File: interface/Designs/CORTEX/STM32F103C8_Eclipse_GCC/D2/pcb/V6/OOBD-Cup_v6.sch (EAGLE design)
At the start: 42 parts, among them IC1 MC34063-SO, IC2 BTM-182, IC3 PCA82C250T, T1 BC817, T100 BC817, T101 BC817, U1 STM32F10XTXU6

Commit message: K-Line interface connected
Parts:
- removed C10: 220pF, rcl:C-EUC0603K
- removed C6: 1µF, rcl:C-EUC0603K
- removed C8: 47µ/35V, cap-master:CP-SV-D
- removed C9: 100nF, rcl:C-EUC0603K
- removed D101: B140, diode:SCHOTTKY-DIODESMD
- removed D102: 1N4148, diode:DIODE-MINIMELF
- removed JP3-OBD1: (no value), jumper:JP4E
- removed L3: 47µH, Inductor-Fastron:07HCP-XXXX-50
- removed L4: 47uH, Inductor-Fastron:PIS2408
- removed R100, R102: 82R, rcl:R-EU_R0603
- removed R104, R109: 4k7, rcl:R-EU_R0603
- removed R108: 10k, rcl:R-EU_R0603
- removed T101: BC817, transistor:BC847
- removed U$1: SI9241AEY, Si9241AEY:SI9241AEY
- added C1: 1µF, rcl:C-EUC0603K
- added C2: 220µF, rc-master:CP_6032-TE-C
- added C3: 220pF, rcl:C-EUC0603K
- added C4: 47µ/35V, cap-master:CP-SV-D
- added C5: 100nF, rcl:C-EUC0603K
- added D2: B140, diode:SCHOTTKY-DIODESMD
- added D3: BAS40, diode:BAS40
- added IC$2: SI9243AEY, Vishay_ISO9141:SI9243AEY
- added JP3: (no value), jumper:JP1E
- added L1: 47uH, Inductor-Fastron:PIS2408
- added L2: 47µH, Inductor-Fastron:07HCP-XXXX-50
- added R11: 3k3, rcl:R-EU_R0603
- added R12, R13, R14: 1R, rcl:R-EU_R0805
- added R15: 5k6, rcl:R-EU_R0603
- added R16: 120R, resistor:R-EU_R0603
- added R18: 510R, resistor:R-EU_R0603
- added T2: BC817, transistor:BC847
- C7: value 220µF -> 10nF; device rc-master:CP_6032-TE-C -> resistor:C-EUC0603
- D1: value BAS40 -> 1N4148; device diode:BAS40 -> diode:DIODE-MINIMELF
- IC1: value MC34063-SO -> PCA82C250T; device mc34063:MC34063-SO -> can:PCA82C250T
- IC3: value PCA82C250T -> MC34063-SO; device can:PCA82C250T -> mc34063:MC34063-SO
- JP1: value SPI / SD-Card -> Program
- JP2: value Program -> SPI / SD-Card
- LED1: value Rt/Gr -> Blue; device led:DUOLED2X5 -> led:LEDSQR5.7X3.2
- LED2: value Blue -> Rt/Gr; device led:LEDSQR5.7X3.2 -> led:DUOLED2X5
- R1: value 180k -> 82R
- R3: value 47k -> 82R
- R4: value 10k -> 4k7
- R5, R6: value 1R -> 10k; device rcl:R-EU_R0805 -> rcl:R-EU_R0603
- R7: value 3k3 -> 4k7
- R8: value 5k6 -> 180k
- R9: value 1R -> 47k; device rcl:R-EU_R0805 -> rcl:R-EU_R0603
- renumbered R101 to R10, R110 to R2, T100 to T3
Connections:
- removed net 12V_DOUT1: C8.+, C9.1, IC1.VCC, R5.2, R6.2, R9.2
- removed net MODE2: R104.1
- removed net N$19: R1.1, R3.2
- removed net N$21: REL1G$2.P
- removed net N$22: REL1G$3.P
- removed net PWM+: JP3-OBD1.3
- removed net PWM-: JP3-OBD1.4
- new net +5V: IC$2.VDD
- new net CAN-RXD: IC1D.RXD
- new net CAN-TXD: IC1D.TXD
- new net CAN_SW: R7.1
- new net N$16: JP3.2, R16.1
- new net N$5: IC1D.CANH, R16.2, REL1G$2.P
- new net REL_DIAG: R8.1, R9.2
- new net RX_K: IC$2.RX_K
- new net RX_L: IC$2.RX_L
- new net TX: IC$2.TX
- new net VBAT: D2.A, IC$2.VBAT, JP2-OBD1.4, R18.2
- net +12V: now also C4.+, C5.1, D1.C, D2.C, IC3.VCC, LED1.A, R12.2, R13.2, R14.2; no longer D101.A, D102.C, JP2-OBD1.4, LED2.A
- net +3V3: now also C1.1, C2.+, JP1.1, L1.P$1, L2.P$1, R15.2; no longer C6.1, C7.+, JP2.1, L3.P$1, L4.P$1, R8.2
- net A0: now also JP2.3; no longer JP1.3
- net BOOT0: now also JP1.2; no longer JP2.2
- net CS: now also JP2.2; no longer JP1.2
- net CTS: now also JP2.5; no longer JP1.5
- net GND: now also C1.2, C2.-, C3.2, C4.-, C5.2, C7.2, D3.A, IC$2.GND, IC1D.RS, IC3.GND, JP1.3, LED2.C, R11.2, R5.2, R6.2, R9.1, T2.E; no longer C10.2, C6.2, C7.-, C8.-, C9.2, D1.A, IC1.GND, JP2.3, LED1.C, R108.2, R3.1, R4.2, R7.2, T101.E
- net K-LINE: now also C7.1, IC$2.K, JP2-OBD1.2, R18.1; no longer JP3-OBD1.2
- net L-LINE: now also IC$2.L, JP2-OBD1.1; no longer JP3-OBD1.1
- net MISO: now also JP2.6; no longer JP1.6
- net MODE1: now also R6.1; no longer R4.1
- net MOSI: now also JP2.8; no longer JP1.8
- net N$10: now also R4.2; no longer R109.2
- net N$11: now also C3.1, IC3.TC; no longer C10.1, IC1.TC
- net N$12: now also IC3.DRC, IC3.IPK, IC3.SWC, R12.1, R13.1, R14.1; no longer IC1.DRC, IC1.IPK, IC1.SWC, R5.1, R6.1, R9.1
- net N$13: now also IC3.CII, R11.1, R15.1; no longer IC1.CII, R7.1, R8.1
- net N$14: now also D3.C, IC3.SWE, L1.P$2, L2.P$2; no longer D1.C, IC1.SWE, L3.P$2, L4.P$2
- net N$20: now also R7.2, T2.B; no longer R104.2, T101.B
- net N$27: now also D1.A, R8.2, T2.C; no longer D102.A, R1.2, T101.C
- net N$3: now also IC1D.CANL, JP3.1, REL1G$3.P; no longer D101.C
- net N$4: now also LED2.AR, R3.2; no longer LED1.AR, R102.2
- net N$6: now also LED2.AG, R1.2; no longer LED1.AG, R100.2
- net N$7: now also LED1.C, R4.1; no longer LED2.C, R109.1
- net RTS: now also JP2.7; no longer JP1.7
- net SCK: now also JP2.4; no longer JP1.4
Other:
- note added: "CAN - Interface"
- note added: "CAN - Transceiver"
- note added: "K - Line"
- note added: "K-Line - Interface"
- note added: "Power Supply / OBD2-Connector"
- note added: "Si9243A"
- note removed: "CAN-Transceiver"
- note removed: "K-Line"
- note removed: "Power Supply"

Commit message: add further parts for STM32F103T8
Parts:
- added C10, C9: 15p, resistor:C-EUC0603
- added C6, C8: 100n, resistor:C-EUC0603
- added IC4: BTM-182, BTM182:BTM-182
- added Q1: 8MHz, crystal:CRYSTALCTS406
- added R17, R19: 10k, resistor:R-EU_R0603
- IC2: value BTM-182 -> 78L05SMD; device BTM182:BTM-182 -> linear:78L05SMD
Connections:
- new net BTM_RX: IC4.UART-RX, JP1.8
- new net BTM_TX: IC4.UART-TX, JP1.6
- new net BT_RES-: IC4.RESETB
- new net N$1: C10.2, Q1.1, U1PORTD/OSC.PD0/OSC<=
- new net N$2: C9.2, Q1.2, U1PORTD/OSC.PD1/OSC=>
- new net RESET-: JP1.4, R17.1, U1RESET.NRST
- new net STM_RXD: JP1.5, U1PORTA_H.PA10
- new net STM_TXD: JP1.7, U1PORTA_H.PA9
- net +12V: now also C6.1, IC2G$1.VIN
- net +3V3: now also IC4.VDD, IC4.VDD_USB, R17.2, U1AN_POWER.VDDA, U1POWER.VDD_1, U1POWER.VDD_2, U1POWER.VDD_3
- net +5V: now also C8.1, IC1P.VCC, IC2G$1.VOUT
- net BOOT0: now also R19.2, U1RESET.BOOT0
- net GND: now also C10.1, C6.2, C8.2, C9.1, IC1P.GND, IC2G$1.GND@1, IC2G$1.GND@2, IC2G$1.GND@3, IC2G$1.GND@4, IC4.GND, R19.1, U1AN_POWER.VSSA, U1POWER.VSS_1, U1POWER.VSS_2, U1POWER.VSS_3
- net MODE1: now also R5.1
- net RX_K: now also U1PORTA_L.PA3
- net TX: now also U1PORTA_L.PA2
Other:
- note added: "Bluetooth - Interface"
- note added: "Bluetooth - Modul (BTM182)"
- note added: "K - Line (Si9243/L9637)"
- note added: "TJA1050/MCP2515/PCA82C250"
- note removed: "Bluetooth Module (BTM182)"
- note removed: "K - Line"
- note removed: "Si9243A"
- note removed: "TJA1050 / MCP2515/ PCA82C250"

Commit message: OOBD-Cup_v6 ready for design review and optimization
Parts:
- removed JP2: SPI / SD-Card, jumper:JP4Q
- added C11: (no value), resistor:C-EUC0603
- added R20: 130k, resistor:R-EU_R0603
- added R21: 27k, resistor:R-EU_R0603
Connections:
- removed net A0: JP2.3, R10.1
- removed net CS: JP2.2
- removed net CTS: JP2.5
- removed net MISO: JP2.6
- removed net MOSI: JP2.8
- removed net N$8: R2.1
- removed net RTS: JP2.7
- removed net SCK: JP2.4
- new net BUZZER: R10.1, U1PORTA_L.PA6
- new net LED1: R3.1, U1PORTB_L.PB5
- new net LED2: R1.1, U1PORTB_L.PB4
- new net LED_BLUE: R2.1, U1PORTA_L.PA7
- new net N$15: C11.1, R20.1, R21.2, U1PORTB_L.PB0
- new net N$18: R5.1, U1PORTA_H.PA14
- net +12V: now also R20.2
- net GND: now also C11.2, R21.1, U1PORTB_L.PB2
- net MODE1: now also U1PORTA_H.PA13; no longer R5.1
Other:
- moved on the sheet: LED1, LED2, R1, R10, R2, R3, R4, R5, R6, SG1, T1, T3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

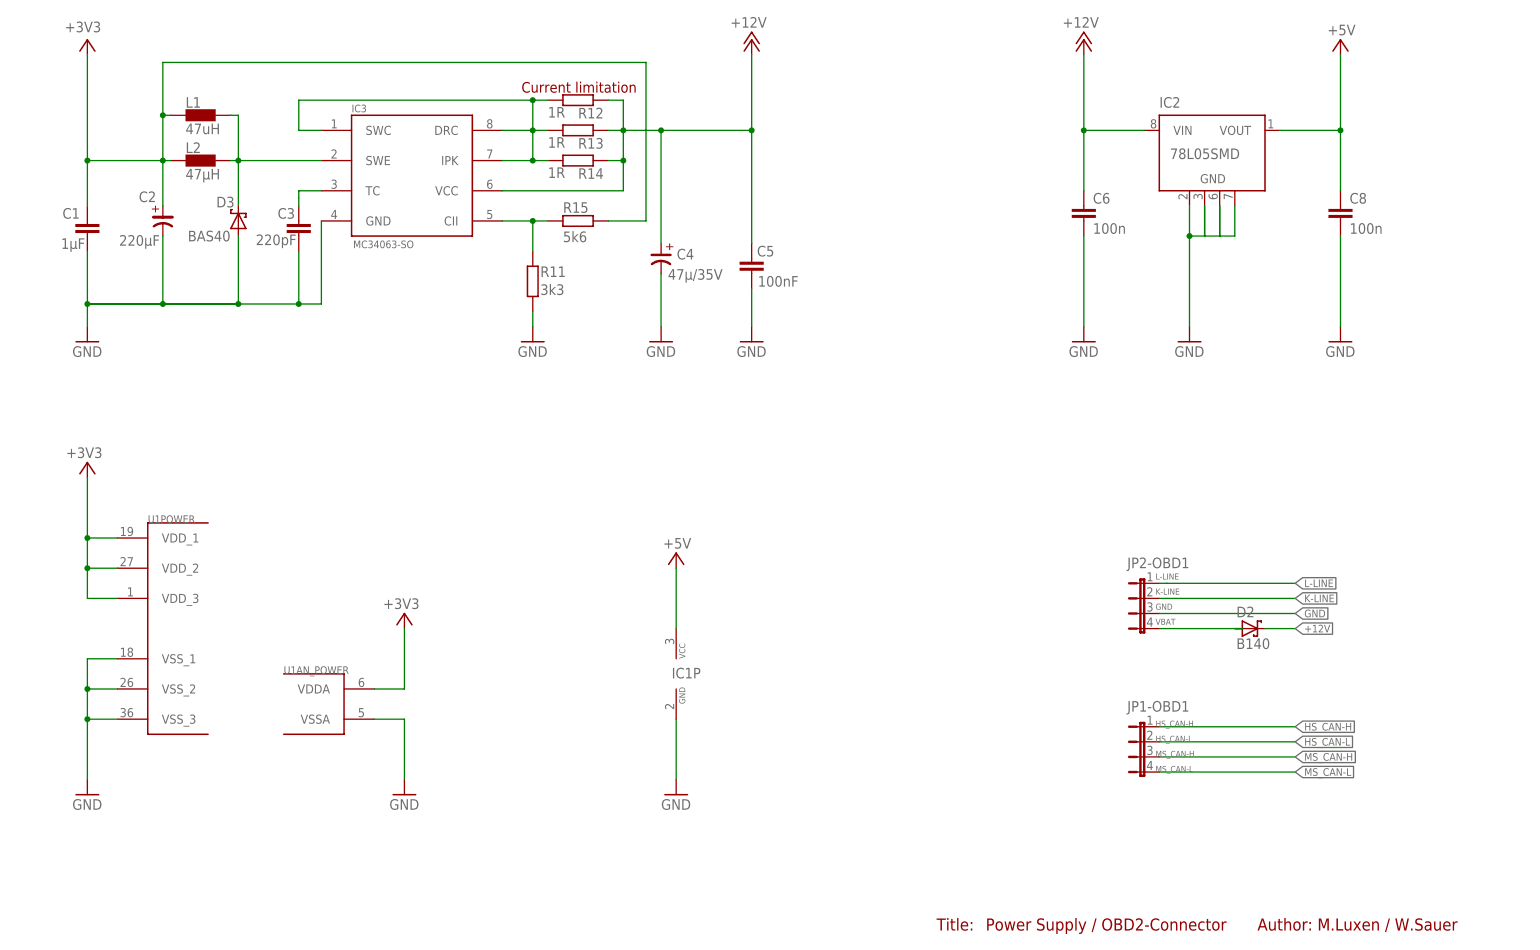
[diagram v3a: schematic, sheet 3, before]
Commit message: connect Relais to STM32 and add further EMC capacitor
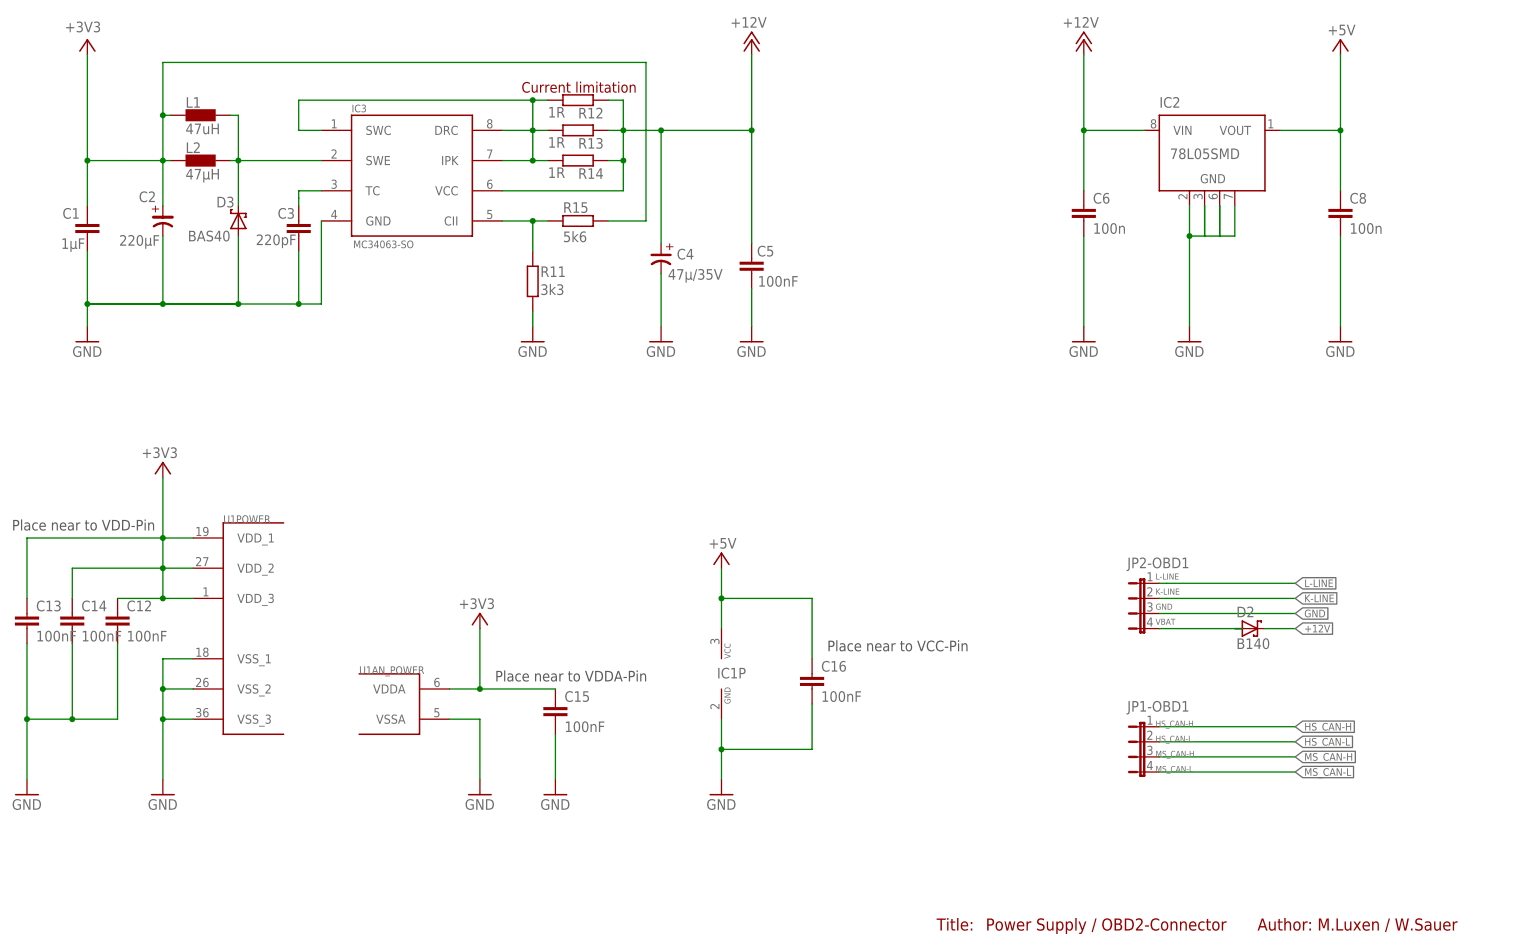
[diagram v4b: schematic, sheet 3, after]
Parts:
- added C12, C13, C14, C15, C16: 100nF, resistor:C-EUC0603
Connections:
- net +3V3: now also C12.1, C13.1, C14.1, C15.1
- net +5V: now also C16.1
- net CAN_SW: now also U1PORTB_L.PB3
- net GND: now also C12.2, C13.2, C14.2, C15.2, C16.2
- net REL_DIAG: now also U1PORTB_L.PB1
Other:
- note added: "Place near to VCC-Pin"
- note added: "Place near to VDD-Pin"
- note added: "Place near to VDDA-Pin"
- moved on the sheet: IC1P, U1AN_POWER, U1POWER

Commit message: add missing parts and doe last modification for first prototypes/batch
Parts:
- added C17: 47µ/35V, cap-master:CP-SV-D
- added C18: 100nF, rcl:C-EUC0603K
- added C19: 100nF, resistor:C-EUC0603
- added C20, C21: 100n, resistor:C-EUC0603
- added IC5: 78L05SMD, linear:78L05SMD
- added R22, R23, R24: 1R, rcl:R-EU_R0805
- added R25: 5k6, rcl:R-EU_R0603
- added T4: BC817, transistor:BC847
- C1: value 1µF -> 100nF; device rcl:C-EUC0603K -> resistor:C-EUC0603
- C10: value 15p -> 100nF
- C11: value (none) -> 100nF
- C12: value 100nF -> 1µF; device resistor:C-EUC0603 -> rcl:C-EUC0603K
- C14: value 100nF -> 220µF; device resistor:C-EUC0603 -> rc-master:CP_6032-TE-C
- C15: value 100nF -> 220pF; device resistor:C-EUC0603 -> rcl:C-EUC0603K
- C2: value 220µF -> 100nF; device rc-master:CP_6032-TE-C -> rcl:C-EUC0603
- C3: value 220pF -> 15p; device rcl:C-EUC0603K -> resistor:C-EUC0603
- C4: value 47µ/35V -> 15p; device cap-master:CP-SV-D -> resistor:C-EUC0603
- C5: device rcl:C-EUC0603K -> rcl:C-EUC0603
- C6: value 100n -> 100nF; device resistor:C-EUC0603 -> rcl:C-EUC0603
- C7: value 10nF -> 100nF
- C8: value 100n -> 100nF
- C9: value 15p -> 10nF
- D2: value B140 -> BAS40; device diode:SCHOTTKY-DIODESMD -> diode:BAS40
- D3: value BAS40 -> B140; device diode:BAS40 -> diode:SCHOTTKY-DIODESMD
- IC1: value PCA82C250T -> 24LC16; device can:PCA82C250T -> microchip:24LC00OT
- IC2: value 78L05SMD -> BTM-182; device linear:78L05SMD -> BTM182:BTM-182
- IC3: value MC34063-SO -> PCA82C250T; device mc34063:MC34063-SO -> can:PCA82C250T
- IC4: value BTM-182 -> MC34063-SO; device BTM182:BTM-182 -> mc34063:MC34063-SO
- L1: value 47uH -> 100uH
- L2: value 47µH -> 100µH
- LED1: value Blue -> Rt/Gr; device led:LEDSQR5.7X3.2 -> led:DUOLED2X5
- LED2: value Rt/Gr -> Blue; device led:DUOLED2X5 -> led:LEDSQR5.7X3.2
- R1: value 82R -> 130k; device rcl:R-EU_R0603 -> resistor:R-EU_R0603
- R11: value 3k3 -> 4k7; device rcl:R-EU_R0603 -> resistor:R-EU_R0603
- R12: value 1R -> 510R; device rcl:R-EU_R0805 -> rcl:R-EU_R0603
- R13, R14: value 1R -> 4k7; device rcl:R-EU_R0805 -> rcl:R-EU_R0603
- R15: value 5k6 -> 4k7
- R16: value 120R -> 4k7; device resistor:R-EU_R0603 -> rcl:R-EU_R0603
- R17: value 10k -> 180k; device resistor:R-EU_R0603 -> rcl:R-EU_R0603
- R18: value 510R -> 47k; device resistor:R-EU_R0603 -> rcl:R-EU_R0603
- R19: value 10k -> 120R
- R2: value 4k7 -> 27k; device rcl:R-EU_R0603 -> resistor:R-EU_R0603
- R20: value 130k -> 510R
- R21: value 27k -> 3k3; device resistor:R-EU_R0603 -> rcl:R-EU_R0603
- R3: value 82R -> 10k; device rcl:R-EU_R0603 -> resistor:R-EU_R0603
- R4: value 4k7 -> 10k; device rcl:R-EU_R0603 -> resistor:R-EU_R0603
- R7: value 4k7 -> 82R
- R8: value 180k -> 82R
- R9: value 47k -> 4k7; device rcl:R-EU_R0603 -> resistor:R-EU_R0603
- renumbered IC$2 to IC$1, JP3 to JP2
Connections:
- removed net RX_L: IC$1.RX_L
- new net N$17: R10.2, T1.B
- new net N$19: IC1.SCL, R9.1, U1PORTB_L.PB6
- new net N$21: IC1.SDA, R11.1, U1PORTB_L.PB7
- new net N$8: R10.1, U1PORTA_L.PA4
- net +12V: now also C17.+, C18.1, C20.1, D3.C, IC4.VCC, IC5G$1.VIN, LED2.A, R1.2, R22.2, R23.2, R24.2; no longer C4.+, C5.1, C6.1, D2.C, IC2G$1.VIN, IC3.VCC, LED1.A, R12.2, R13.2, R14.2, R20.2
- net +3V3: now also C10.1, C11.1, C14.+, C16.1, C2.1, C5.1, C6.1, IC1.VCC, IC2.VDD, IC2.VDD_USB, R11.2, R25.2, R3.2, R9.2; no longer C1.1, C14.1, C15.1, C2.+, IC4.VDD, IC4.VDD_USB, R15.2, R17.2
- net +5V: now also C19.1, C21.1, C7.1, IC3P.VCC, IC5G$1.VOUT; no longer C16.1, C8.1, IC1P.VCC, IC2G$1.VOUT
- net BOOT0: now also R4.2; no longer R19.2
- net BTM_RX: now also IC2.UART-RX; no longer IC4.UART-RX
- net BTM_TX: now also IC2.UART-TX; no longer IC4.UART-TX
- net BT_RES-: now also IC2.RESETB, U1PORTA_H.PA15; no longer IC4.RESETB
- net BUZZER: now also R14.1; no longer R10.1
- net CAN-RXD: now also IC3D.RXD, U1PORTA_H.PA11; no longer IC1D.RXD
- net CAN-TXD: now also IC3D.TXD, U1PORTA_H.PA12; no longer IC1D.TXD
- net CAN_SW: now also R16.1; no longer R7.1
- net GND: now also C10.2, C14.-, C17.-, C18.2, C19.2, C2.2, C20.2, C21.2, C3.1, C4.1, C9.2, D2.A, IC1.GND, IC2.GND, IC3D.RS, IC3P.GND, IC5G$1.GND@1, IC5G$1.GND@2, IC5G$1.GND@3, IC5G$1.GND@4, LED1.C, R18.1, R2.1, R21.2, R4.1, T4.E; no longer C10.1, C14.2, C2.-, C3.2, C4.-, C9.1, D3.A, IC1D.RS, IC1P.GND, IC2G$1.GND@1, IC2G$1.GND@2, IC2G$1.GND@3, IC2G$1.GND@4, IC3.GND, LED2.C, R11.2, R19.1, R21.1, R9.1
- net K-LINE: now also C9.1, R20.1; no longer C7.1, R18.1
- net L-LINE: now also R12.1, T1.C; no longer IC$1.L
- net LED1: now also R8.1; no longer R3.1
- net LED2: now also R7.1; no longer R1.1
- net LED_BLUE: now also R13.1; no longer R2.1
- net N$1: now also C4.2; no longer C10.2
- net N$10: now also R15.2, T2.C; no longer R4.2, T1.C
- net N$11: now also C15.1, IC4.TC; no longer C3.1, IC3.TC
- net N$12: now also IC4.DRC, IC4.IPK, IC4.SWC, R22.1, R23.1, R24.1; no longer IC3.DRC, IC3.IPK, IC3.SWC, R12.1, R13.1, R14.1
- net N$13: now also IC4.CII, R21.1, R25.1; no longer IC3.CII, R11.1, R15.1
- net N$14: now also D2.C, IC4.SWE; no longer D3.C, IC3.SWE
- net N$15: now also C1.1, R1.1, R2.2; no longer C11.1, R20.1, R21.2
- net N$16: now also R19.1; no longer R16.1
- net N$2: now also C3.2; no longer C9.2
- net N$20: now also R16.2, T4.B; no longer R7.2, T2.B
- net N$24: now also R14.2; no longer R10.2
- net N$27: now also R17.2, T4.C; no longer R8.2, T2.C
- net N$3: now also IC3D.CANL; no longer IC1D.CANL
- net N$4: now also LED1.AR, R8.2; no longer LED2.AR, R3.2
- net N$5: now also IC3D.CANH, R19.2; no longer IC1D.CANH, R16.2
- net N$6: now also LED1.AG, R7.2; no longer LED2.AG, R1.2
- net N$7: now also LED2.C, R15.1; no longer LED1.C, R4.1
- net N$9: now also R13.2, T2.B; no longer R2.2, T1.B
- net REL_DIAG: now also R17.1, R18.2; no longer R8.1, R9.2
- net RESET-: now also R3.1; no longer R17.1
- net VBAT: now also C8.1, D3.A, R12.2, R20.2; no longer D2.A, R18.2
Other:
- note added: "16k I2C EE-PROM"
- note added: "Alternative Footprint"
- note added: "Boot1"
- note added: "Low ESR"
- note added: "OOBD-Cup v6"
- note added: "Place near to VDD pin"
- note added: "R5"
- note added: "R6"
- note added: "Vbat"
- note removed: "R108"
- note removed: "R4"
